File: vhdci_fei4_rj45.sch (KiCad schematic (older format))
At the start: 45 parts, among them J1 71430-015, J10 Lemo, J11 Lemo, J12 Lemo, J2 RJ45, J24 GS2, J3 RJ45, J4 RJ45, J5 RJ45, J6 RJ45, J7 RJ45, J8 RJ45, J9 RJ45, P1 USB_OTG, U1 LM317_SOT223

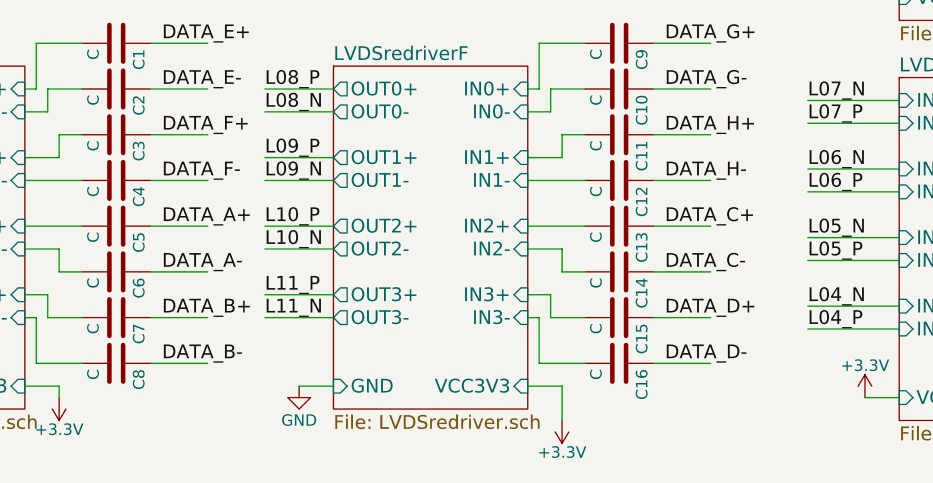
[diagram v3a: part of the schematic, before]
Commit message: Route 2 level shifters
Signed-off-by: katie dunne <kedunne@lbl.gov>
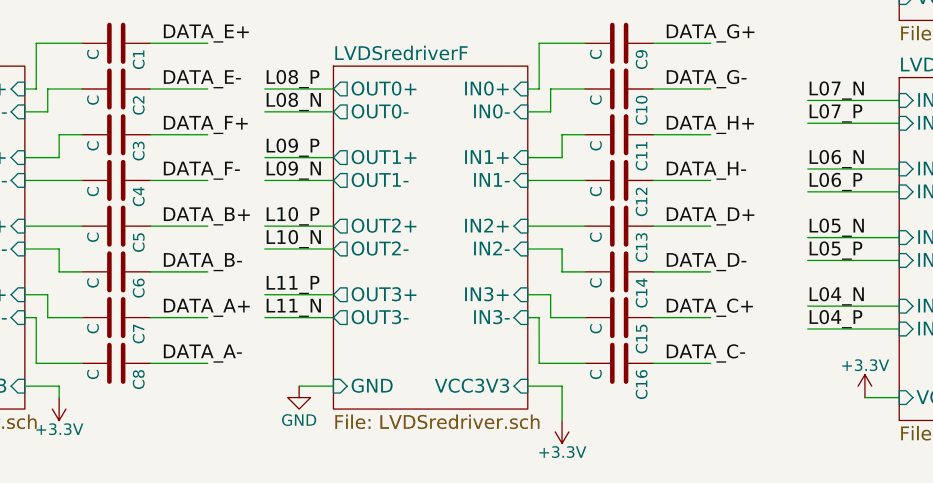
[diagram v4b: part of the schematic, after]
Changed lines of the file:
@@
 EESchema Schematic File Version 2
 LIBS:vhdci_fei4_rj45-rescue
+LIBS:ds90lv004
+LIBS:con-molex-vhdci
 LIBS:power
 LIBS:device
@@
 LIBS:contrib
 LIBS:valves
+LIBS:module
 LIBS:vhdci_fei4_rj45-cache
 EELAYER 25 0
@@
 Text Label 2350 6500 0    60   ~ 0
 DATA_F-
+Text Label 2350 7100 0    60   ~ 0
+DATA_A+
+Text Label 2350 7300 0    60   ~ 0
+DATA_A-
 Text Label 2350 6700 0    60   ~ 0
-DATA_A+
+DATA_B+
 Text Label 2350 6900 0    60   ~ 0
-DATA_A-
-Text Label 2350 7100 0    60   ~ 0
-DATA_B+
-Text Label 2350 7300 0    60   ~ 0
 DATA_B-
 Text Label 4550 5900 0    60   ~ 0
@@
 Text Label 4550 6500 0    60   ~ 0
 DATA_H-
+Text Label 4550 7100 0    60   ~ 0
+DATA_C+
+Text Label 4550 7300 0    60   ~ 0
+DATA_C-
 Text Label 4550 6700 0    60   ~ 0
-DATA_C+
+DATA_D+
 Text Label 4550 6900 0    60   ~ 0
-DATA_C-
-Text Label 4550 7100 0    60   ~ 0
-DATA_D+
-Text Label 4550 7300 0    60   ~ 0
 DATA_D-
 Text Label 7350 800  0    60   ~ 0
@@
 $EndComp
 $Comp
-L +3.3V #PWR029
+L +3.3V #PWR028
 U 1 1 59196164
 P 3800 4925
-F 0 "#PWR029" H 3800 4775 50  0001 C CNN
+F 0 "#PWR028" H 3800 4775 50  0001 C CNN
 F 1 "+3.3V" H 3800 5065 50  0000 C CNN
 F 2 "" H 3800 4925 50  0000 C CNN
@@
 $EndComp
 $Comp
-L +5V #PWR030
+L +5V #PWR029
 U 1 1 5919616B
 P 3800 4675
-F 0 "#PWR030" H 3800 4525 50  0001 C CNN
+F 0 "#PWR029" H 3800 4525 50  0001 C CNN
 F 1 "+5V" H 3800 4815 50  0000 C CNN
 F 2 "" H 3800 4675 50  0000 C CNN
@@
 Connection ~ 4875 1625
 $Comp
-L GND #PWR028
+L GND #PWR030
 U 1 1 59195614
 P 4900 3475
-F 0 "#PWR028" H 4900 3225 50  0001 C CNN
+F 0 "#PWR030" H 4900 3225 50  0001 C CNN
 F 1 "GND" H 4900 3325 50  0000 C CNN
 F 2 "" H 4900 3475 50  0001 C CNN
